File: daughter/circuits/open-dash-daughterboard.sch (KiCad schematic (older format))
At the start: 6 parts, among them J1 Conn_02x09_Odd_Even, J2 Molex_Mini-Fit_Jr_5566, J3 Molex_Mini-Fit_Jr_5566, J4 Molex_Mini-Fit_Jr_5566, U1 radio-housing-mounts

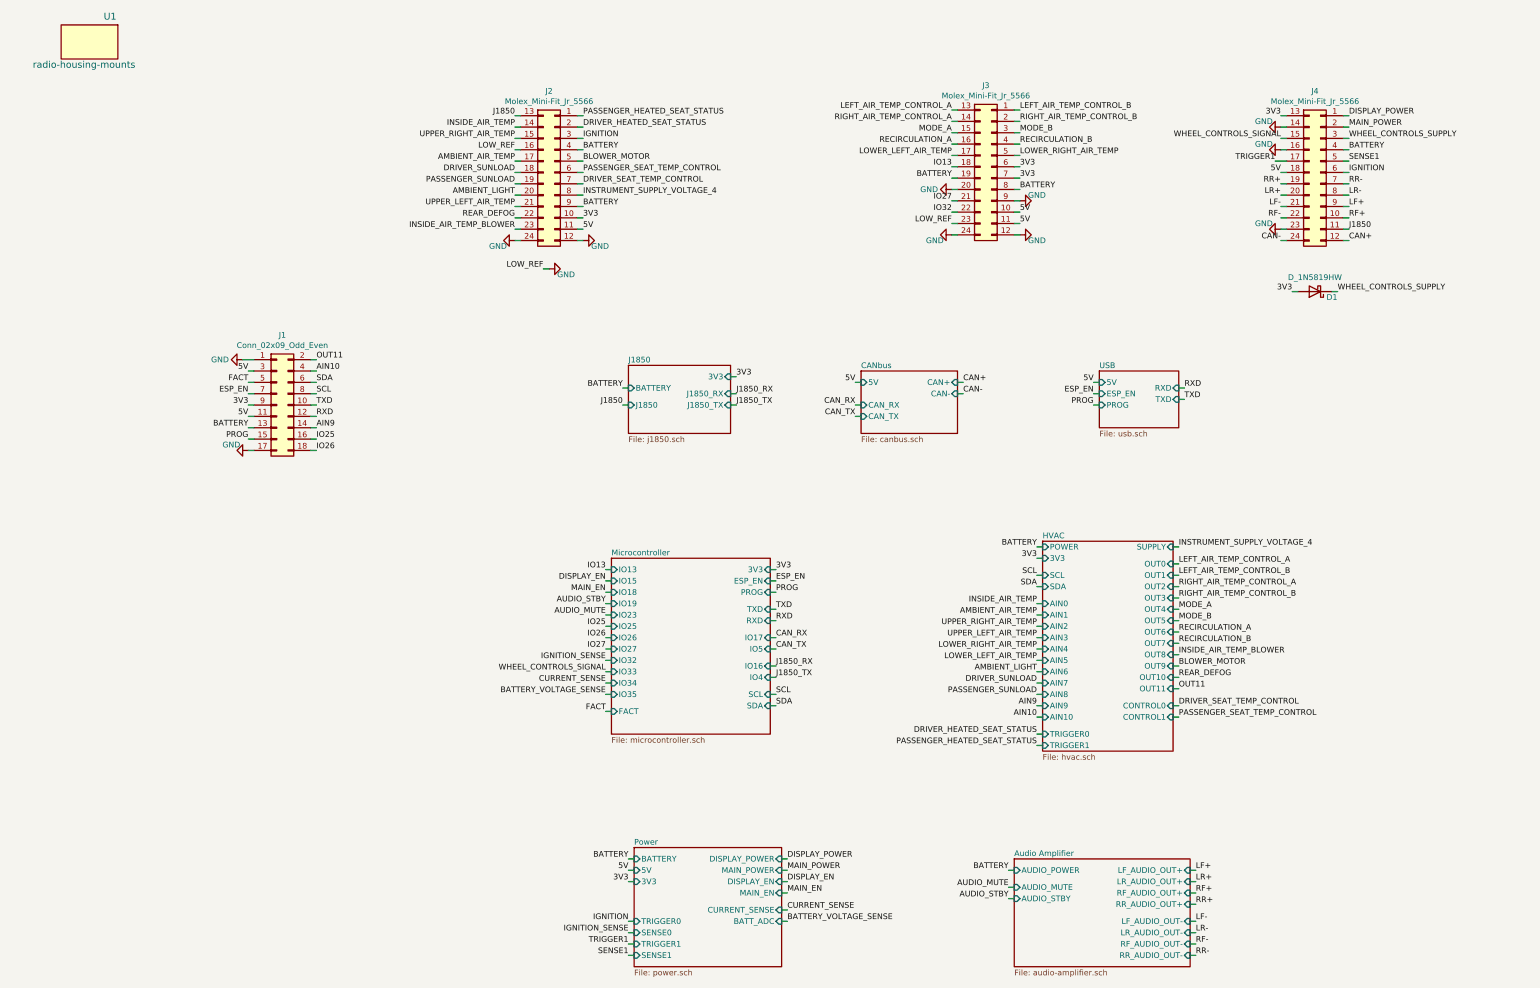
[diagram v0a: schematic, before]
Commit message: 0) Switched to h-bridge drivers for hvac 1) Connected ignition sense io 2) MCP config pins and reset 3) Fixed usb resistors 4) Fixed BJT footprint 5) Added car interface pcb for C6 Corvette
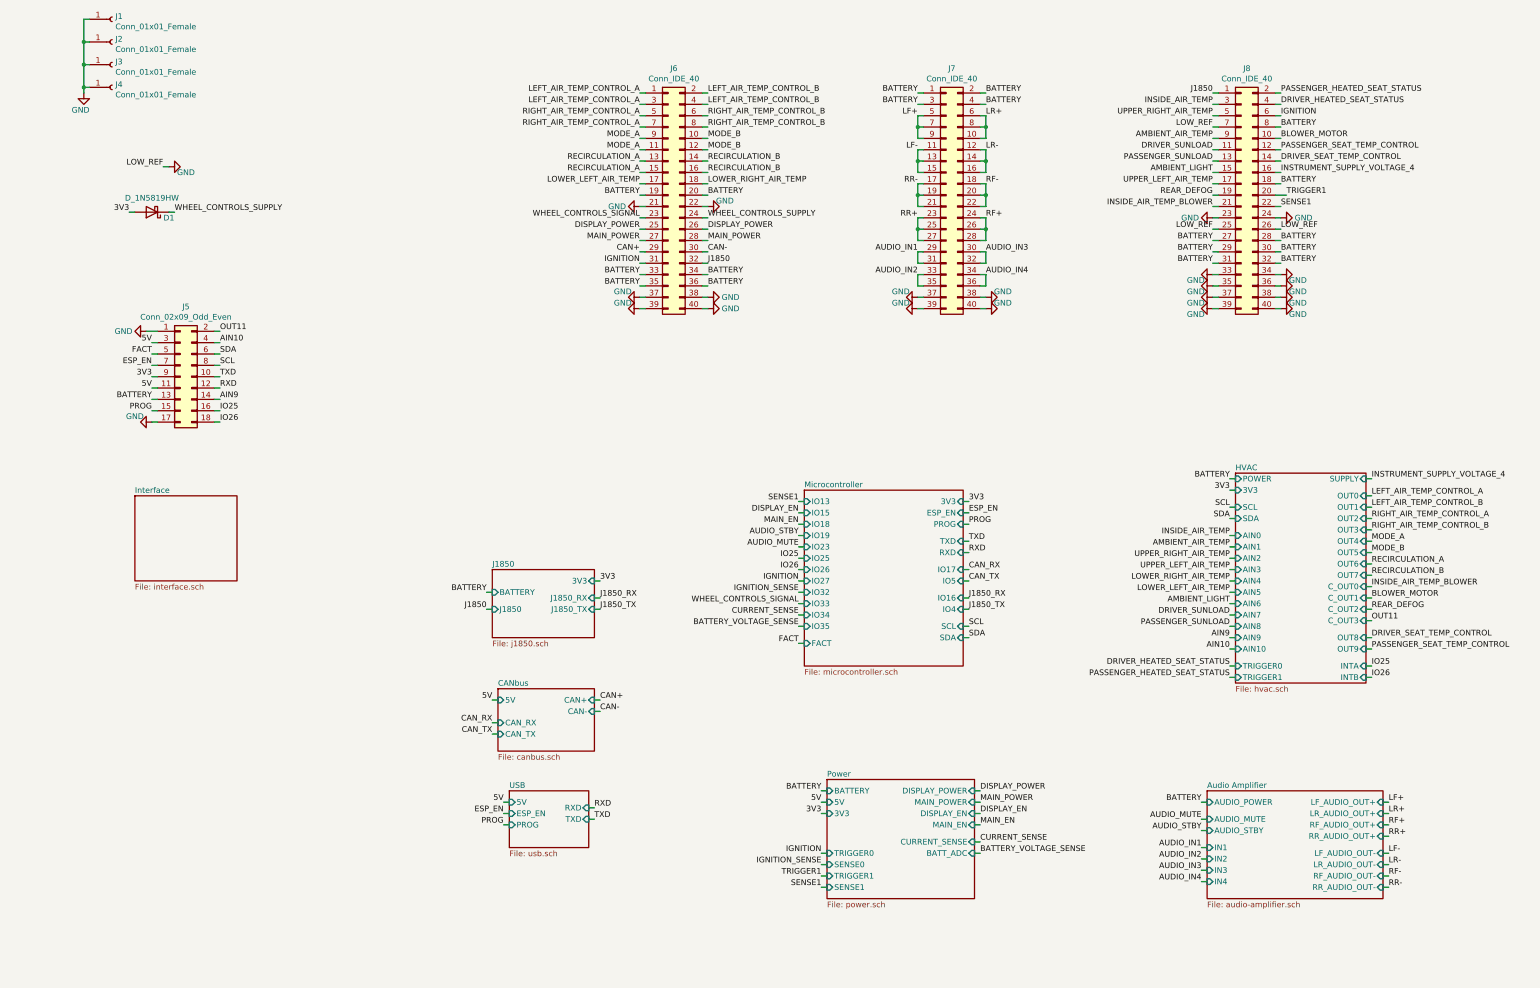
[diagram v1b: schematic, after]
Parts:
- removed J2, J3, J4: Molex_Mini-Fit_Jr_5566, Connector_Molex:Molex_Mini-Fit_Jr_5566-24A2_2x12_P4.20mm_Vertical, symbol open-dash-daughterboard-rescue:Molex_Mini-Fit_Jr_5566-Open_Automation
- removed U1: radio-housing-mounts, Open_Automation:radio-housing-mounts, symbol open-dash-daughterboard-rescue:radio-housing-mounts-Open_Automation
- added J1, J2, J3, J4: Conn_01x01_Female, Open_Automation:Mount_Hole, symbol Connector:Conn_01x01_Female
- added J6, J7, J8: Conn_IDE_40, Connector_IDC:IDC-Header_2x20_P2.54mm_Vertical, symbol Open_Automation:Conn_IDE_40
- renumbered J1 to J5
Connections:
- net AMBIENT_AIR_TEMP: now also J8.9 (Pin_9)
- net AMBIENT_LIGHT: now also J8.15 (Pin_15)
- net BATTERY: now also J6.19 (Pin_19), J6.20 (Pin_20), J6.33 (Pin_33), J6.34 (Pin_34), J6.35 (Pin_35), J6.36 (Pin_36), J7.1 (Pin_1), J7.2 (Pin_2), J7.3 (Pin_3), J7.4 (Pin_4), J8.18 (Pin_18), J8.27 (Pin_27), J8.28 (Pin_28), J8.29 (Pin_29), J8.30 (Pin_30), J8.31 (Pin_31), J8.32 (Pin_32), J8.8 (Pin_8)
- net BLOWER_MOTOR: now also J8.10 (Pin_10)
- net CAN+: now also J6.29 (Pin_29)
- net CAN-: now also J6.30 (Pin_30)
- net DISPLAY_POWER: now also J6.25 (Pin_25), J6.26 (Pin_26)
- net DRIVER_HEATED_SEAT_STATUS: now also J8.4 (Pin_4)
- net DRIVER_SEAT_TEMP_CONTROL: now also J8.14 (Pin_14)
- net DRIVER_SUNLOAD: now also J8.11 (Pin_11)
- net GND: now also J1.1 (Pin_1), J2.1 (Pin_1), J3.1 (Pin_1), J4.1 (Pin_1), J6.21 (Pin_21), J6.22 (Pin_22), J6.37 (Pin_37), J6.38 (Pin_38), J6.39 (Pin_39), J6.40 (Pin_40), J7.37 (Pin_37), J7.38 (Pin_38), J7.39 (Pin_39), J7.40 (Pin_40), J8.23 (Pin_23), J8.24 (Pin_24), J8.25 (Pin_25), J8.26 (Pin_26), J8.33 (Pin_33), J8.34 (Pin_34), J8.35 (Pin_35), J8.36 (Pin_36), J8.37 (Pin_37), J8.38 (Pin_38), J8.39 (Pin_39), J8.40 (Pin_40), J8.7 (Pin_7)
- net IGNITION: now also J6.31 (Pin_31), J8.6 (Pin_6)
- net INSIDE_AIR_TEMP: now also J8.3 (Pin_3)
- net INSIDE_AIR_TEMP_BLOWER: now also J8.21 (Pin_21)
- net INSTRUMENT_SUPPLY_VOLTAGE_4: now also J8.16 (Pin_16)
- net J1850: now also J6.32 (Pin_32), J8.1 (Pin_1)
- net LEFT_AIR_TEMP_CONTROL_A: now also J6.1 (Pin_1), J6.3 (Pin_3)
- net LEFT_AIR_TEMP_CONTROL_B: now also J6.2 (Pin_2), J6.4 (Pin_4)
- net LF+: now also J7.5 (Pin_5), J7.7 (Pin_7), J7.9 (Pin_9)
- net LF-: now also J7.11 (Pin_11), J7.13 (Pin_13), J7.15 (Pin_15)
- net LOWER_LEFT_AIR_TEMP: now also J6.17 (Pin_17)
- net LOWER_RIGHT_AIR_TEMP: now also J6.18 (Pin_18)
- net LR+: now also J7.10 (Pin_10), J7.6 (Pin_6), J7.8 (Pin_8)
- net LR-: now also J7.12 (Pin_12), J7.14 (Pin_14), J7.16 (Pin_16)
- net MAIN_POWER: now also J6.27 (Pin_27), J6.28 (Pin_28)
- net MODE_A: now also J6.11 (Pin_11), J6.9 (Pin_9)
- net MODE_B: now also J6.10 (Pin_10), J6.12 (Pin_12)
- net PASSENGER_HEATED_SEAT_STATUS: now also J8.2 (Pin_2)
- net PASSENGER_SEAT_TEMP_CONTROL: now also J8.12 (Pin_12)
- net PASSENGER_SUNLOAD: now also J8.13 (Pin_13)
- net REAR_DEFOG: now also J8.19 (Pin_19)
- net RECIRCULATION_A: now also J6.13 (Pin_13), J6.15 (Pin_15)
- net RECIRCULATION_B: now also J6.14 (Pin_14), J6.16 (Pin_16)
- net RF+: now also J7.24 (Pin_24), J7.26 (Pin_26), J7.28 (Pin_28)
- net RF-: now also J7.18 (Pin_18), J7.20 (Pin_20), J7.22 (Pin_22)
- net RIGHT_AIR_TEMP_CONTROL_A: now also J6.5 (Pin_5), J6.7 (Pin_7)
- net RIGHT_AIR_TEMP_CONTROL_B: now also J6.6 (Pin_6), J6.8 (Pin_8)
- net RR+: now also J7.23 (Pin_23), J7.25 (Pin_25), J7.27 (Pin_27)
- net RR-: now also J7.17 (Pin_17), J7.19 (Pin_19), J7.21 (Pin_21)
- net SENSE1: now also J8.22 (Pin_22)
- net TRIGGER1: now also J8.20 (Pin_20)
- net UPPER_LEFT_AIR_TEMP: now also J8.17 (Pin_17)
- net UPPER_RIGHT_AIR_TEMP: now also J8.5 (Pin_5)
- net WHEEL_CONTROLS_SIGNAL: now also J6.23 (Pin_23)
- net WHEEL_CONTROLS_SUPPLY: now also J6.24 (Pin_24)
- new net AUDIO_IN1: J7.29 (Pin_29), J7.31 (Pin_31)
- new net AUDIO_IN2: J7.33 (Pin_33), J7.35 (Pin_35)
- new net AUDIO_IN3: J7.30 (Pin_30), J7.32 (Pin_32)
- new net AUDIO_IN4: J7.34 (Pin_34), J7.36 (Pin_36)
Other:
- moved on the sheet: D1, J5

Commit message: finished schematic, working on layout
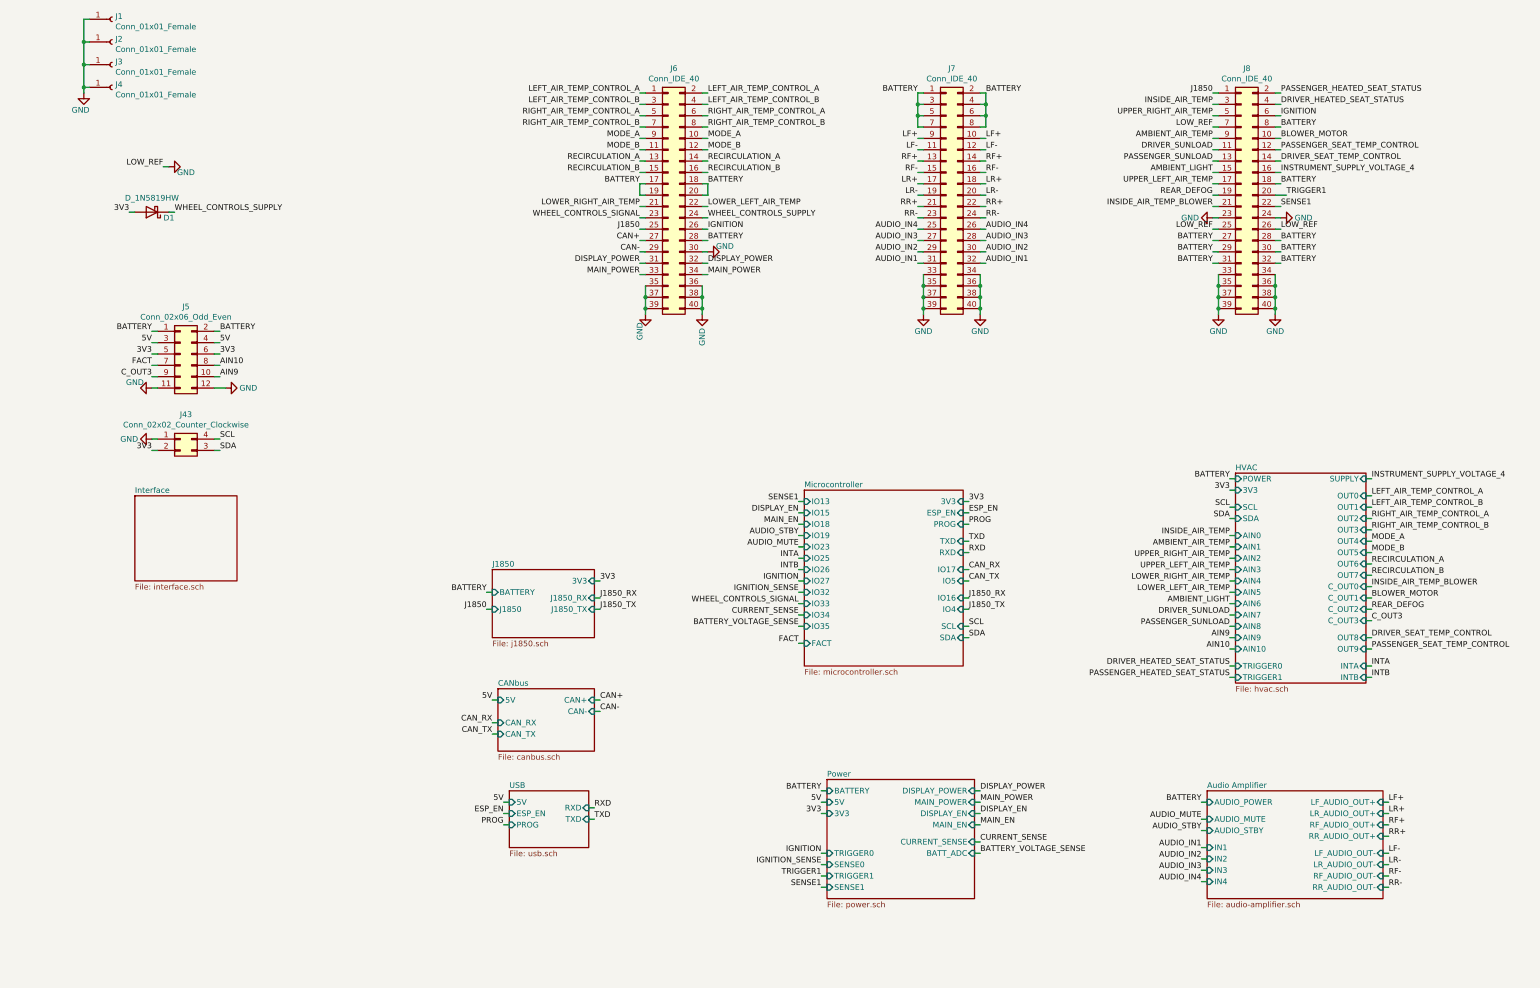
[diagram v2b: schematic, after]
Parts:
- removed J5: Conn_02x09_Odd_Even, Connector_PinHeader_2.54mm:PinHeader_2x09_P2.54mm_Vertical_SMD, symbol open-dash-daughterboard-rescue:Conn_02x09_Odd_Even-Connector_Generic
- added J43: Conn_02x02_Counter_Clockwise, Connector_PinHeader_2.54mm:PinHeader_2x02_P2.54mm_Vertical_SMD, symbol open-dash-daughterboard-rescue:Conn_02x02_Counter_Clockwise-Connector_Generic
- added J5: Conn_02x06_Odd_Even, Connector_PinHeader_2.54mm:PinHeader_2x06_P2.54mm_Vertical_SMD, symbol Connector_Generic:Conn_02x06_Odd_Even
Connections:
- net 3V3: now also J43.2 (Pin_2), J5.5 (Pin_5), J5.6 (Pin_6)
- net 5V: now also J5.3 (Pin_3), J5.4 (Pin_4)
- net AIN10: now also J5.8 (Pin_8)
- net AIN9: now also J5.10 (Pin_10)
- net AUDIO_IN1: now also J7.32 (Pin_32); no longer J7.29 (Pin_29)
- net AUDIO_IN2: now also J7.29 (Pin_29), J7.30 (Pin_30); no longer J7.33 (Pin_33), J7.35 (Pin_35)
- net AUDIO_IN3: now also J7.27 (Pin_27), J7.28 (Pin_28); no longer J7.30 (Pin_30), J7.32 (Pin_32)
- net AUDIO_IN4: now also J7.25 (Pin_25), J7.26 (Pin_26); no longer J7.34 (Pin_34), J7.36 (Pin_36)
- net BATTERY: now also J6.17 (Pin_17), J6.18 (Pin_18), J6.28 (Pin_28), J7.5 (Pin_5), J7.6 (Pin_6), J7.7 (Pin_7), J7.8 (Pin_8), J5.1 (Pin_1), J5.2 (Pin_2); no longer J6.33 (Pin_33), J6.34 (Pin_34), J6.35 (Pin_35), J6.36 (Pin_36)
- net CAN+: now also J6.27 (Pin_27); no longer J6.29 (Pin_29)
- net CAN-: now also J6.29 (Pin_29); no longer J6.30 (Pin_30)
- net DISPLAY_POWER: now also J6.31 (Pin_31), J6.32 (Pin_32); no longer J6.25 (Pin_25), J6.26 (Pin_26)
- net FACT: now also J5.7 (Pin_7)
- net GND: now also J6.30 (Pin_30), J6.35 (Pin_35), J6.36 (Pin_36), J7.33 (Pin_33), J7.34 (Pin_34), J7.35 (Pin_35), J7.36 (Pin_36), J43.1 (Pin_1), J5.11 (Pin_11), J5.12 (Pin_12); no longer J6.21 (Pin_21), J6.22 (Pin_22)
- net IGNITION: now also J6.26 (Pin_26); no longer J6.31 (Pin_31)
- net J1850: now also J6.25 (Pin_25); no longer J6.32 (Pin_32)
- net LEFT_AIR_TEMP_CONTROL_A: now also J6.2 (Pin_2); no longer J6.3 (Pin_3)
- net LEFT_AIR_TEMP_CONTROL_B: now also J6.3 (Pin_3); no longer J6.2 (Pin_2)
- net LF+: now also J7.10 (Pin_10); no longer J7.5 (Pin_5), J7.7 (Pin_7)
- net LF-: now also J7.12 (Pin_12); no longer J7.13 (Pin_13), J7.15 (Pin_15)
- net LOWER_LEFT_AIR_TEMP: now also J6.22 (Pin_22); no longer J6.17 (Pin_17)
- net LOWER_RIGHT_AIR_TEMP: now also J6.21 (Pin_21); no longer J6.18 (Pin_18)
- net LR+: now also J7.17 (Pin_17), J7.18 (Pin_18); no longer J7.10 (Pin_10), J7.6 (Pin_6), J7.8 (Pin_8)
- net LR-: now also J7.19 (Pin_19), J7.20 (Pin_20); no longer J7.12 (Pin_12), J7.14 (Pin_14), J7.16 (Pin_16)
- net MAIN_POWER: now also J6.33 (Pin_33), J6.34 (Pin_34); no longer J6.27 (Pin_27), J6.28 (Pin_28)
- net MODE_A: now also J6.10 (Pin_10); no longer J6.11 (Pin_11)
- net MODE_B: now also J6.11 (Pin_11); no longer J6.10 (Pin_10)
- net RECIRCULATION_A: now also J6.14 (Pin_14); no longer J6.15 (Pin_15)
- net RECIRCULATION_B: now also J6.15 (Pin_15); no longer J6.14 (Pin_14)
- net RF+: now also J7.13 (Pin_13), J7.14 (Pin_14); no longer J7.24 (Pin_24), J7.26 (Pin_26), J7.28 (Pin_28)
- net RF-: now also J7.15 (Pin_15), J7.16 (Pin_16); no longer J7.18 (Pin_18), J7.20 (Pin_20), J7.22 (Pin_22)
- net RIGHT_AIR_TEMP_CONTROL_A: now also J6.6 (Pin_6); no longer J6.7 (Pin_7)
- net RIGHT_AIR_TEMP_CONTROL_B: now also J6.7 (Pin_7); no longer J6.6 (Pin_6)
- net RR+: now also J7.21 (Pin_21), J7.22 (Pin_22); no longer J7.23 (Pin_23), J7.25 (Pin_25), J7.27 (Pin_27)
- net RR-: now also J7.23 (Pin_23), J7.24 (Pin_24); no longer J7.17 (Pin_17), J7.19 (Pin_19), J7.21 (Pin_21)
- net SCL: now also J43.4 (Pin_4)
- net SDA: now also J43.3 (Pin_3)
- new net C_OUT3: J5.9 (Pin_9)

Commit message: finished layout
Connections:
- net LF+: now also J7.17 (Pin_17), J7.18 (Pin_18); no longer J7.10 (Pin_10), J7.9 (Pin_9)
- net LF-: now also J7.19 (Pin_19), J7.20 (Pin_20); no longer J7.11 (Pin_11), J7.12 (Pin_12)
- net LR+: now also J7.15 (Pin_15), J7.16 (Pin_16); no longer J7.17 (Pin_17), J7.18 (Pin_18)
- net LR-: now also J7.13 (Pin_13), J7.14 (Pin_14); no longer J7.19 (Pin_19), J7.20 (Pin_20)
- net RF+: now also J7.21 (Pin_21), J7.22 (Pin_22); no longer J7.13 (Pin_13), J7.14 (Pin_14)
- net RF-: now also J7.23 (Pin_23), J7.24 (Pin_24); no longer J7.15 (Pin_15), J7.16 (Pin_16)
- net RR+: now also J7.11 (Pin_11), J7.12 (Pin_12); no longer J7.21 (Pin_21), J7.22 (Pin_22)
- net RR-: now also J7.10 (Pin_10), J7.9 (Pin_9); no longer J7.23 (Pin_23), J7.24 (Pin_24)
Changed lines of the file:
@@
 F11 "AUDIO_POWER" I L 11000 7700 50
 F12 "AUDIO_MUTE" I L 11000 7850 50
-F13 "IN2" I L 11000 8200 50
-F14 "IN4" I L 11000 8400 50
-F15 "IN3" I L 11000 8300 50
-F16 "IN1" I L 11000 8100 50
+F13 "AMP_IN2" I L 11000 8200 50
+F14 "AMP_IN4" I L 11000 8400 50
+F15 "AMP_IN3" I L 11000 8300 50
+F16 "AMP_IN1" I L 11000 8100 50
 $EndSheet
 Text Label 12600 7700 0    50   ~ 0
@@
 	7400 6150 7450 6150
 Wire Wire Line
-	7400 5750 7450 5750
-Wire Wire Line
 	7450 5650 7400 5650
 Wire Wire Line
@@
 Text Label 7400 5850 2    50   ~ 0
 IGNITION_SENSE
-Text Label 7400 5750 2    50   ~ 0
-IGNITION
 Text Label 7400 5050 2    50   ~ 0
 SENSE1
@@
 Wire Wire Line
 	11650 2950 11600 2950
-Text Label 8450 2550 2    50   ~ 0
+Text Label 8450 1850 2    50   ~ 0
 RR-
 Wire Wire Line
 	8450 2150 8500 2150
-Text Label 8450 2250 2    50   ~ 0
+Text Label 8450 2150 2    50   ~ 0
 LR+
 Wire Wire Line
@@
 Wire Wire Line
 	9050 1550 9000 1550
-Text Label 8450 2150 2    50   ~ 0
-RF-
 Wire Wire Line
 	8450 2550 8500 2550
@@
 Wire Wire Line
 	8450 2450 8500 2450
-Text Label 8450 1850 2    50   ~ 0
+Text Label 8450 2250 2    50   ~ 0
 LF+
-Text Label 8450 2350 2    50   ~ 0
+Text Label 8450 2050 2    50   ~ 0
 LR-
 $Comp
@@
 Wire Wire Line
 	6050 2850 6000 2850
-Text Label 8450 1950 2    50   ~ 0
+Text Label 8450 2350 2    50   ~ 0
 LF-
 Wire Wire Line
@@
 Wire Wire Line
 	6600 2550 6550 2550
-$Sheet
-S 1550 5000 900  750
-U 657571BE
-F0 "Interface" 50
-F1 "interface.sch" 50
-$EndSheet
 $Comp
 L Open_Automation:Conn_IDE_40 J6
@@
 	1    0    0    -1
 $EndComp
+Text Label 8450 1950 2    50   ~ 0
+RR+
 Text Label 8450 2450 2    50   ~ 0
-RR+
-Text Label 8450 2050 2    50   ~ 0
 RF+
 Wire Wire Line
@@
 	9050 1550 9050 1450
 Connection ~ 9050 1550
-Text Label 9050 2550 0    50   ~ 0
-RR-
-Wire Wire Line
-	9050 2150 9000 2150
-Text Label 9050 2250 0    50   ~ 0
-LR+
-Wire Wire Line
-	9050 1850 9000 1850
-Text Label 9050 2150 0    50   ~ 0
-RF-
-Wire Wire Line
-	9050 2550 9000 2550
-Wire Wire Line
-	9050 2450 9000 2450
-Text Label 9050 1850 0    50   ~ 0
-LF+
-Text Label 9050 2350 0    50   ~ 0
-LR-
-Text Label 9050 1950 0    50   ~ 0
-LF-
-Text Label 9050 2450 0    50   ~ 0
-RR+
-Text Label 9050 2050 0    50   ~ 0
-RF+
-Wire Wire Line
-	9050 1950 9000 1950
-Wire Wire Line
-	9050 2050 9000 2050
-Wire Wire Line
-	9050 2250 9000 2250
-Wire Wire Line
-	9050 2350 9000 2350
 Wire Wire Line
 	6550 1750 6600 1750
@@
 Wire Wire Line
 	1700 3850 1750 3850
+$Sheet
+S 1550 5000 900  750
+U 657571BE
+F0 "Interface" 50
+F1 "interface.sch" 50
+$EndSheet
+Text Label 8450 2550 2    50   ~ 0
+RF-
+Text Label 9050 1850 0    50   ~ 0
+RR-
+Wire Wire Line
+	9050 2150 9000 2150
+Text Label 9050 2150 0    50   ~ 0
+LR+
+Wire Wire Line
+	9050 1850 9000 1850
+Wire Wire Line
+	9050 2550 9000 2550
+Wire Wire Line
+	9050 2450 9000 2450
+Text Label 9050 2250 0    50   ~ 0
+LF+
+Text Label 9050 2050 0    50   ~ 0
+LR-
+Text Label 9050 2350 0    50   ~ 0
+LF-
+Text Label 9050 1950 0    50   ~ 0
+RR+
+Text Label 9050 2450 0    50   ~ 0
+RF+
+Wire Wire Line
+	9050 1950 9000 1950
+Wire Wire Line
+	9050 2050 9000 2050
+Wire Wire Line
+	9050 2250 9000 2250
+Wire Wire Line
+	9050 2350 9000 2350
+Text Label 9050 2550 0    50   ~ 0
+RF-
 $EndSCHEMATC

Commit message: sent v1.2 to fab
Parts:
- removed D1: D_1N5819HW, Diode_SMD:D_SOD-123, symbol open-dash-daughterboard-rescue:D_1N5819HW-Open_Automation
- added D1: D_1N5819HW, Diode_SMD:D_SOD-123, symbol Open_Automation:D_1N5819HW
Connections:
- net 3V3: now also D1.2 (A)
- net WHEEL_CONTROLS_SUPPLY: now also D1.1 (K)
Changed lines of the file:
@@
 Wire Wire Line
 	1850 2100 1800 2100
-$Comp
-L open-dash-daughterboard-rescue:D_1N5819HW-Open_Automation D1
-U 1 1 5FC75BB4
-P 1700 2500
-F 0 "D1" H 1550 2550 50  0000 C CNN
-F 1 "D_1N5819HW" H 1700 2375 50  0000 C CNN
-F 2 "Diode_SMD:D_SOD-123" H 1700 2325 50  0001 C CNN
-F 3 "http://www.diodes.com/_files/datasheets/ds23022.pdf" H 1700 2500 50  0001 C CNN
-F 4 "https://www.digikey.com/product-detail/en/diodes-incorporated/1N5819HW-7-F/1N5819HW-FDICT-ND/815283" H 1800 2700 50  0001 C CNN "Website"
-F 5 "1N5819HW-7-F" H 1700 2800 50  0001 C CNN "Part Number"
-F 6 "C117948" H -10250 -700 50  0001 C CNN "LCSC"
-	1    1700 2500
-	-1   0    0    1
-$EndComp
 Text Label 2300 3650 0    50   ~ 0
 5V
@@
 Text Label 9050 2550 0    50   ~ 0
 RF-
+$Comp
+L Open_Automation:D_1N5819HW D1
+U 1 1 6076B14B
+P 1700 2500
+F 0 "D1" H 1700 2284 50  0000 C CNN
+F 1 "D_1N5819HW" H 1700 2375 50  0000 C CNN
+F 2 "Diode_SMD:D_SOD-123" H 1700 2325 50  0001 C CNN
+F 3 "https://datasheet.lcsc.com/szlcsc/Diodes-Incorporated-1N5819HW-7-F_C82544.pdf" H 1700 2500 50  0001 C CNN
+F 4 "1N5819HW-7-F" H 1700 2800 50  0001 C CNN "Part Number"
+F 5 "C82544" H 1700 2900 50  0001 C CNN "LCSC"
+	1    1700 2500
+	-1   0    0    1
+$EndComp
 $EndSCHEMATC
